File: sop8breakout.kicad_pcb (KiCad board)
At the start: 2 copper layers, 64.3 x 49.2 mm, 27 parts, among them IC1 MCP6002, IC2 MCP6002, IC3 MCP6002, IC4 MCP6002, IC5 MCP6002, IC6 MCP6002, IC7 MCP6002, IC8 MCP6002, IC9 MCP6002, P1 CONN_01X04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

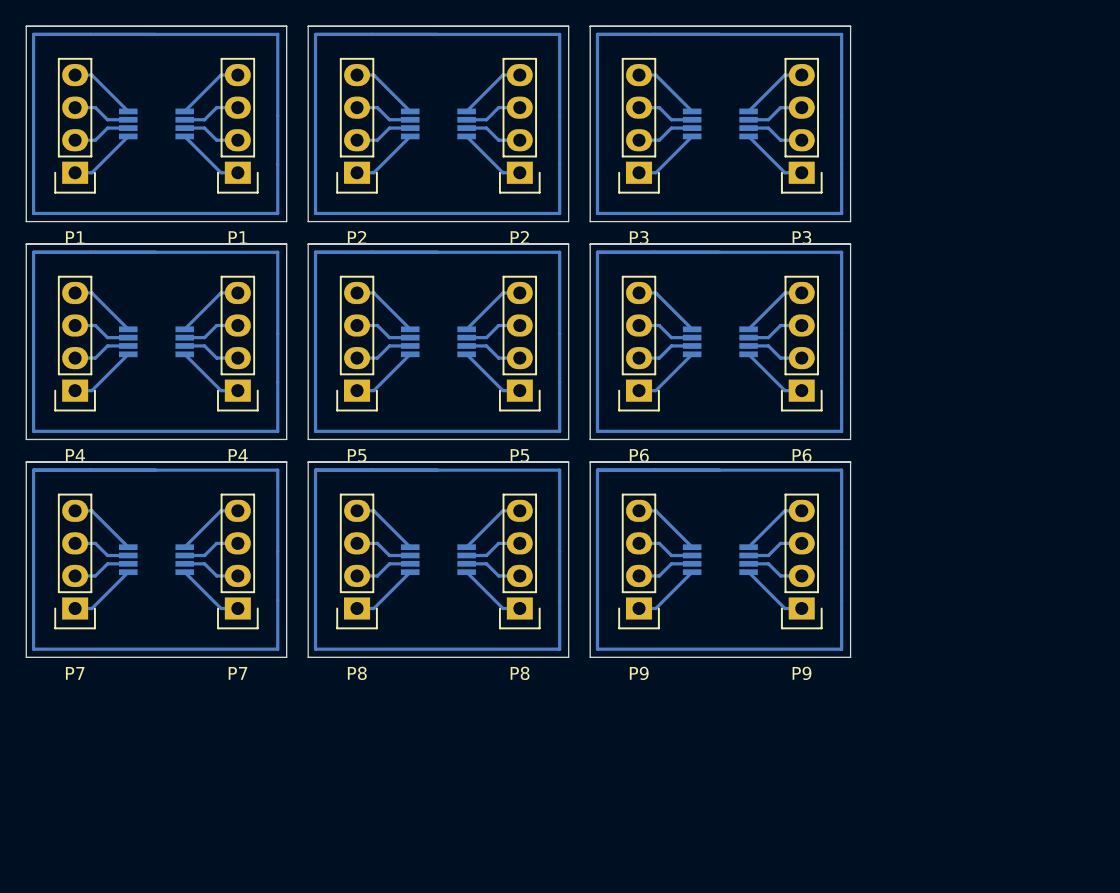
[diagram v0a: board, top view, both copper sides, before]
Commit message: Upon fabrication, we have discovered this is not a SOP-8 socket at all.
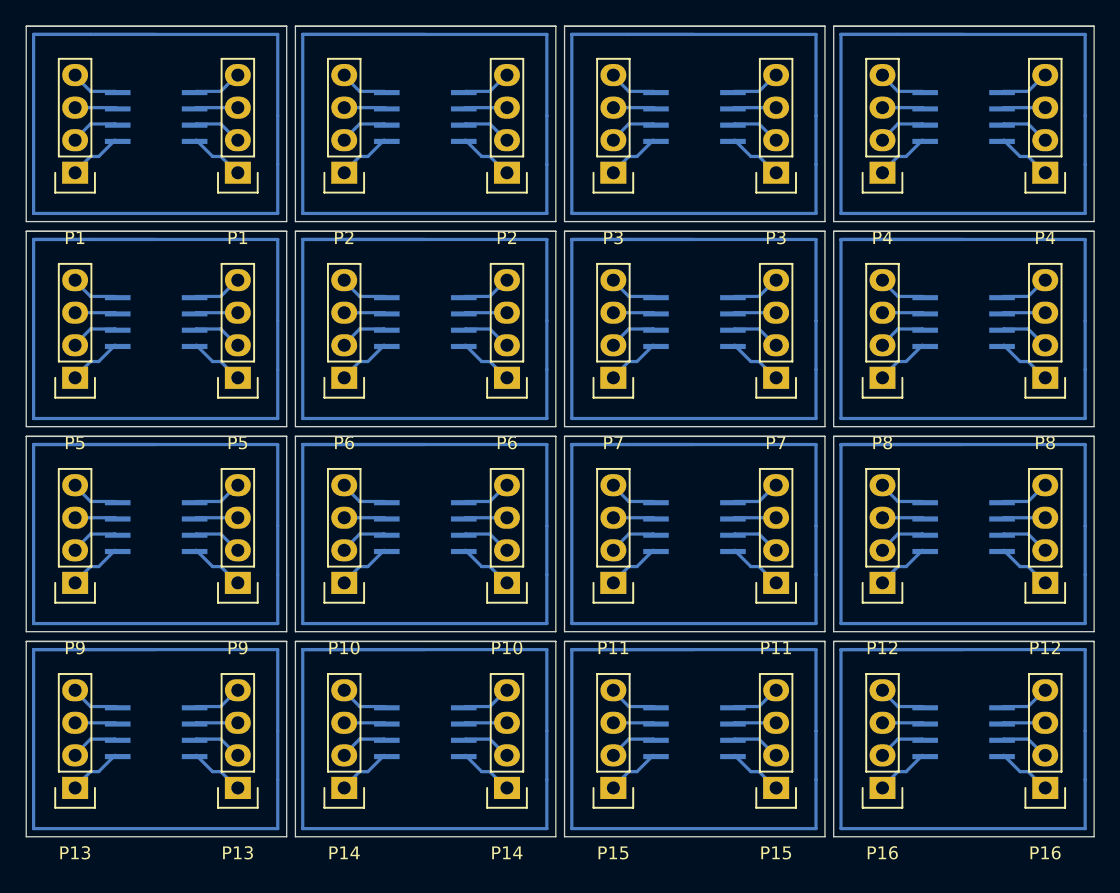
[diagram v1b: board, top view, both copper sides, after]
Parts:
- removed the P2 at (164.3, 109.2)
- removed the P2 at (177.0, 109.2)
- removed the P3 at (186.3, 109.2)
- removed the P3 at (199.0, 109.2)
- removed the P4 at (142.3, 126.2)
- removed the P4 at (155.0, 126.2)
- removed the P5 at (164.3, 126.2)
- removed the P5 at (177.0, 126.2)
- removed the P6 at (186.3, 126.2)
- removed the P6 at (199.0, 126.2)
- removed the P7 at (142.3, 143.2)
- removed the P7 at (155.0, 143.2)
- removed the P8 at (164.3, 143.2)
- removed the P8 at (177.0, 143.2)
- removed the P9 at (186.3, 143.2)
- removed the P9 at (199.0, 143.2)
- added IC10: MCP6002, sop8:SOP-8, B.Cu at (172.1, 139.3)
- added IC11: MCP6002, sop8:SOP-8, B.Cu at (193.1, 139.3)
- added IC12: MCP6002, sop8:SOP-8, B.Cu at (214.1, 139.3)
- added IC13: MCP6002, sop8:SOP-8, B.Cu at (151.1, 155.3)
- added IC14: MCP6002, sop8:SOP-8, B.Cu at (172.1, 155.3)
- added IC15: MCP6002, sop8:SOP-8, B.Cu at (193.1, 155.3)
- added IC16: MCP6002, sop8:SOP-8, B.Cu at (214.1, 155.3)
- added P10: CONN_01X04, Pin_Headers:Pin_Header_Straight_1x04, F.Cu at (176.0, 141.2)
- added P10: CONN_01X04, Pin_Headers:Pin_Header_Straight_1x04, F.Cu at (163.3, 141.2)
- added P11: CONN_01X04, Pin_Headers:Pin_Header_Straight_1x04, F.Cu at (197.0, 141.2)
- added P11: CONN_01X04, Pin_Headers:Pin_Header_Straight_1x04, F.Cu at (184.3, 141.2)
- added P12: CONN_01X04, Pin_Headers:Pin_Header_Straight_1x04, F.Cu at (218.0, 141.2)
- added P12: CONN_01X04, Pin_Headers:Pin_Header_Straight_1x04, F.Cu at (205.3, 141.2)
- added P13: CONN_01X04, Pin_Headers:Pin_Header_Straight_1x04, F.Cu at (155.0, 157.2)
- added P13: CONN_01X04, Pin_Headers:Pin_Header_Straight_1x04, F.Cu at (142.3, 157.2)
- added P14: CONN_01X04, Pin_Headers:Pin_Header_Straight_1x04, F.Cu at (176.0, 157.2)
- added P14: CONN_01X04, Pin_Headers:Pin_Header_Straight_1x04, F.Cu at (163.3, 157.2)
- added P15: CONN_01X04, Pin_Headers:Pin_Header_Straight_1x04, F.Cu at (197.0, 157.2)
- added P15: CONN_01X04, Pin_Headers:Pin_Header_Straight_1x04, F.Cu at (184.3, 157.2)
- added P16: CONN_01X04, Pin_Headers:Pin_Header_Straight_1x04, F.Cu at (218.0, 157.2)
- added P16: CONN_01X04, Pin_Headers:Pin_Header_Straight_1x04, F.Cu at (205.3, 157.2)
- added P2: CONN_01X04, Pin_Headers:Pin_Header_Straight_1x04, F.Cu at (176.0, 109.2)
- added P2: CONN_01X04, Pin_Headers:Pin_Header_Straight_1x04, F.Cu at (163.3, 109.2)
- added P3: CONN_01X04, Pin_Headers:Pin_Header_Straight_1x04, F.Cu at (197.0, 109.2)
- added P3: CONN_01X04, Pin_Headers:Pin_Header_Straight_1x04, F.Cu at (184.3, 109.2)
- added P4: CONN_01X04, Pin_Headers:Pin_Header_Straight_1x04, F.Cu at (218.0, 109.2)
- added P4: CONN_01X04, Pin_Headers:Pin_Header_Straight_1x04, F.Cu at (205.3, 109.2)
- added P5: CONN_01X04, Pin_Headers:Pin_Header_Straight_1x04, F.Cu at (155.0, 125.2)
- added P5: CONN_01X04, Pin_Headers:Pin_Header_Straight_1x04, F.Cu at (142.3, 125.2)
- added P6: CONN_01X04, Pin_Headers:Pin_Header_Straight_1x04, F.Cu at (176.0, 125.2)
- added P6: CONN_01X04, Pin_Headers:Pin_Header_Straight_1x04, F.Cu at (163.3, 125.2)
- added P7: CONN_01X04, Pin_Headers:Pin_Header_Straight_1x04, F.Cu at (197.0, 125.2)
- added P7: CONN_01X04, Pin_Headers:Pin_Header_Straight_1x04, F.Cu at (184.3, 125.2)
- added P8: CONN_01X04, Pin_Headers:Pin_Header_Straight_1x04, F.Cu at (218.0, 125.2)
- added P8: CONN_01X04, Pin_Headers:Pin_Header_Straight_1x04, F.Cu at (205.3, 125.2)
- added P9: CONN_01X04, Pin_Headers:Pin_Header_Straight_1x04, F.Cu at (155.0, 141.2)
- added P9: CONN_01X04, Pin_Headers:Pin_Header_Straight_1x04, F.Cu at (142.3, 141.2)
- IC1, IC2, IC3, IC4, IC5, IC6, IC7, IC8, IC9: footprint Housings_SSOP:MSOP-8_3x3mm_Pitch0.65mm -> sop8:SOP-8
- moved IC4 67.2 mm to (214.1, 107.3), turned to 90 degrees
- moved IC7 47.3 mm to (193.1, 123.3), turned to 90 degrees
- moved IC8 46.4 mm to (214.1, 123.3), turned to 90 degrees
- moved IC9 41.5 mm to (151.1, 139.3), turned to 90 degrees
- moved IC6 20.5 mm to (172.1, 123.3), turned to 90 degrees
- moved IC5 19.5 mm to (151.1, 123.3), turned to 90 degrees
- moved IC1 3.12 mm to (151.1, 107.3), turned to 90 degrees
- moved IC2 2.41 mm to (172.1, 107.3), turned to 90 degrees
- moved IC3 1.96 mm to (193.1, 107.3), turned to 90 degrees
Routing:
- net (no net): track 680.1 -> 1209.0 mm
- net Net-(IC1-Pad1): track 47.9 -> 72.4 mm
- net Net-(IC1-Pad8): track 47.9 -> 71.3 mm
- net Net-(IC1-Pad2): track 40.9 -> 64.0 mm
- net Net-(IC1-Pad7): track 40.9 -> 62.9 mm
- net Net-(IC1-Pad4): track 47.9 -> 64.0 mm
- net Net-(IC1-Pad5): track 47.9 -> 62.9 mm
- net Net-(IC1-Pad6): track 40.9 -> 54.5 mm
- net Net-(IC1-Pad3): track 40.9 -> 53.5 mm
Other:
- board size 64.3 x 49.2 mm -> 83.3 x 63.2 mm
